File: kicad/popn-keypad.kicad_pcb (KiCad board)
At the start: 2 copper layers, 133.3 x 47.6 mm, 14 parts, among them U1 Arduino_Pro_Micro

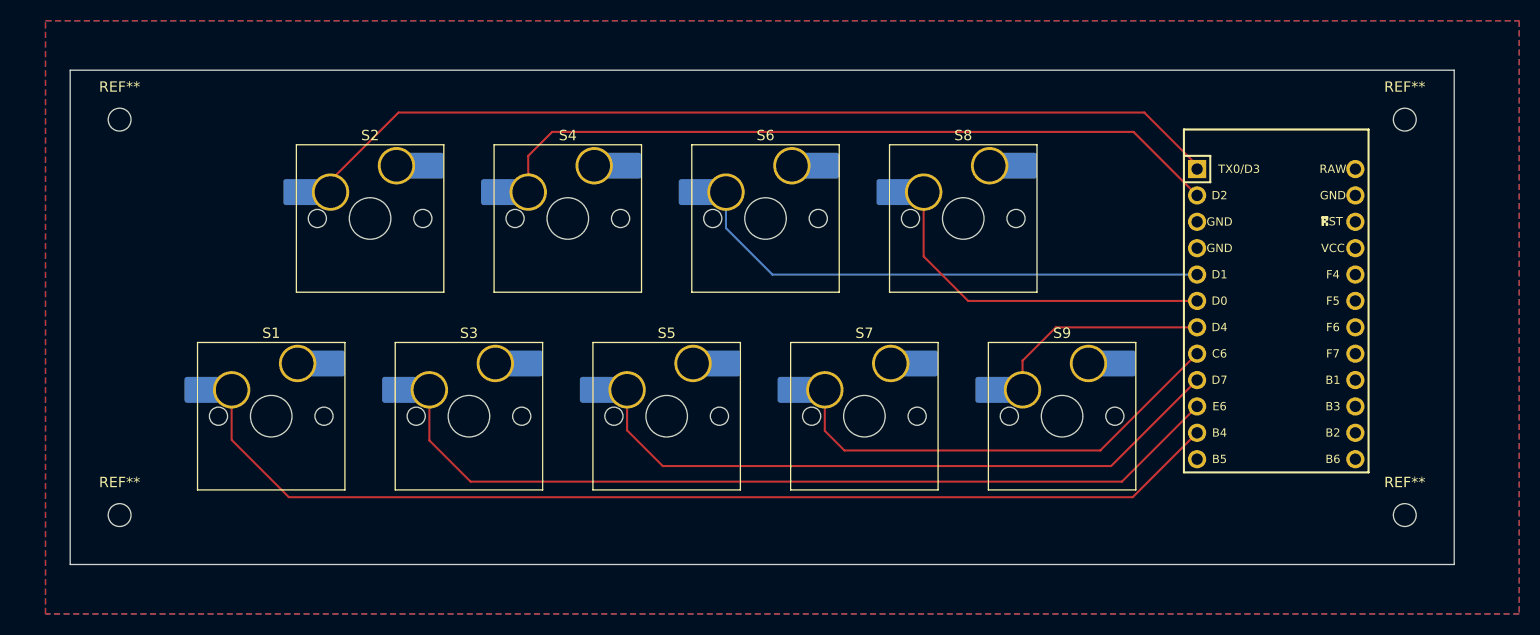
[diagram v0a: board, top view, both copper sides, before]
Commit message: Redesigned board
Moved the microcontroller farther away from the keys. Also re-routed my traces to be further from any holes on the board.
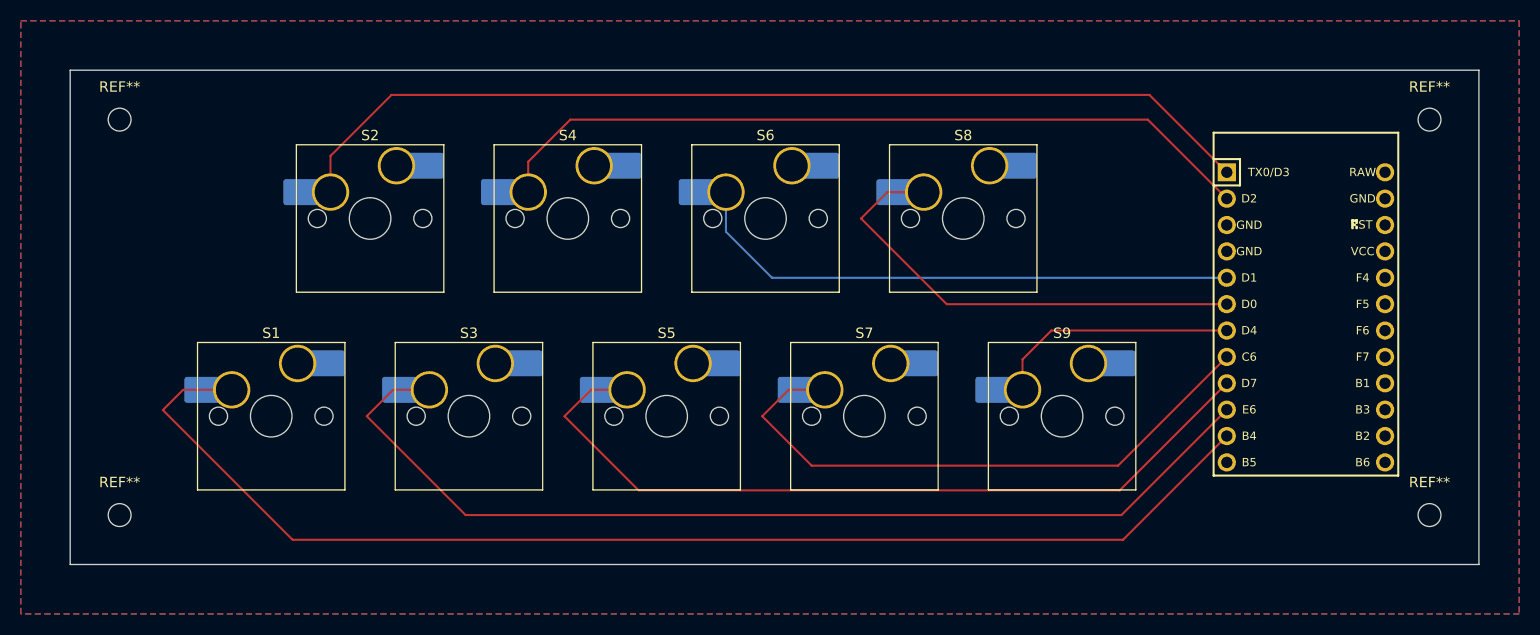
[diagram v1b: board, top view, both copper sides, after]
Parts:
- moved U1 2.88 mm to (209.4, 85.7)
- moved REF** 2.38 mm to (221.3, 66.6)
- moved REF** 2.38 mm to (221.3, 104.7)
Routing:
- net S9: track 102.7 -> 119.2 mm
- net S8: track 83.4 -> 98.0 mm
- net S7: track 63.7 -> 78.1 mm
- net S6: track 44.4 -> 58.1 mm
- net S4: track 34.3 -> 45.7 mm
- net S1: track 89.7 -> 96.4 mm
- net S2: track 71.4 -> 75.0 mm
- net S3: track 50.8 -> 53.9 mm
- net S5: track 20.9 -> 23.8 mm
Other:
- board size 133.3 x 47.6 mm -> 135.7 x 47.6 mm
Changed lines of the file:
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@@
 	(footprint "MountingHole:MountingHole_2.2mm_M2"
 		(layer "F.Cu")
-		(at 218.96 66.64)
+		(at 221.34 66.64)
 		(descr "Mounting Hole 2.2mm, M2, no annular, generated by kicad-footprint-generator mountinghole.py")
 		(tags "mountinghole M2")
@@
 	(footprint "ScottoKeebs_MCU:Arduino_Pro_Micro"
 		(layer "F.Cu")
-		(at 206.58 85.37)
+		(at 209.44 85.68)
 		(property "Reference" "U1"
 			(at 0 1.625 0)
@@
 	(footprint "MountingHole:MountingHole_2.2mm_M2"
 		(layer "F.Cu")
-		(at 218.96 104.72)
+		(at 221.34 104.72)
 		(descr "Mounting Hole 2.2mm, M2, no annular, generated by kicad-footprint-generator mountinghole.py")
 		(tags "mountinghole M2")
@@
 	(gr_rect
 		(start 90.44 61.88)
-		(end 223.72 109.48)
+		(end 226.1 109.48)
 		(stroke
 			(width 0.05)
@@
 	)
 	(segment
-		(start 115.51 72.51)
-		(end 122.062796 65.957204)
+		(start 115.51 73.62)
+		(end 115.51 70.13)
 		(width 0.2)
 		(layer "F.Cu")
@@
 	)
 	(segment
-		(start 193.876204 65.957204)
-		(end 198.96 71.041)
+		(start 121.38 64.26)
+		(end 194.37 64.26)
 		(width 0.2)
 		(layer "F.Cu")
@@
 	)
 	(segment
-		(start 122.062796 65.957204)
-		(end 193.876204 65.957204)
+		(start 115.51 70.13)
+		(end 121.38 64.26)
 		(width 0.2)
 		(layer "F.Cu")
@@
 	)
 	(segment
-		(start 198.96 71.041)
-		(end 198.96 71.4)
+		(start 194.37 64.26)
+		(end 201.82 71.71)
 		(width 0.2)
 		(layer "F.Cu")
@@
 	)
 	(segment
-		(start 153.59 73.62)
-		(end 153.59 77.09)
+		(start 158.03 81.87)
+		(end 201.82 81.87)
 		(width 0.2)
 		(layer "B.Cu")
@@
 	)
 	(segment
-		(start 153.59 77.09)
-		(end 158.06 81.56)
+		(start 153.59 73.62)
+		(end 153.59 77.43)
 		(width 0.2)
 		(layer "B.Cu")
@@
 	)
 	(segment
-		(start 158.06 81.56)
-		(end 198.96 81.56)
+		(start 153.59 77.43)
+		(end 158.03 81.87)
 		(width 0.2)
 		(layer "B.Cu")
@@
 	)
 	(segment
-		(start 182.15 89.85)
-		(end 185.36 86.64)
+		(start 182.15 89.725)
+		(end 184.925 86.95)
 		(width 0.2)
 		(layer "F.Cu")
@@
 	(segment
 		(start 182.15 92.66)
-		(end 182.15 89.85)
+		(end 182.15 89.725)
 		(width 0.2)
 		(layer "F.Cu")
@@
 	)
 	(segment
-		(start 185.36 86.64)
-		(end 198.96 86.64)
+		(start 184.925 86.95)
+		(end 201.82 86.95)
 		(width 0.2)
 		(layer "F.Cu")
@@
 	)
 	(segment
-		(start 147.5 100)
-		(end 144.07 96.57)
+		(start 138.04 95.2)
+		(end 140.58 92.66)
 		(width 0.2)
 		(layer "F.Cu")
@@
 	)
 	(segment
-		(start 198.96 91.72)
-		(end 190.68 100)
+		(start 201.82 92.03)
+		(end 191.51 102.34)
 		(width 0.2)
 		(layer "F.Cu")
@@
 	)
 	(segment
-		(start 190.68 100)
-		(end 147.5 100)
+		(start 140.58 92.66)
+		(end 144.07 92.66)
 		(width 0.2)
 		(layer "F.Cu")
@@
 	)
 	(segment
-		(start 144.07 96.57)
-		(end 144.07 92.66)
+		(start 145.18 102.34)
+		(end 138.04 95.2)
+		(width 0.2)
+		(layer "F.Cu")
+		(net 5)
+	)
+	(segment
+		(start 191.51 102.34)
+		(end 145.18 102.34)
 		(width 0.2)
 		(layer "F.Cu")
@@
 	)
 	(segment
-		(start 192.76 103)
-		(end 111.5 103)
+		(start 99.365 94.605)
+		(end 101.31 92.66)
 		(width 0.2)
 		(layer "F.Cu")
@@
 	)
 	(segment
-		(start 111.5 103)
-		(end 105.99 97.49)
+		(start 111.86 107.1)
+		(end 99.365 94.605)
 		(width 0.2)
 		(layer "F.Cu")
@@
 	)
 	(segment
-		(start 198.96 96.8)
-		(end 192.76 103)
+		(start 201.82 97.11)
+		(end 191.83 107.1)
 		(width 0.2)
 		(layer "F.Cu")
@@
 	)
 	(segment
-		(start 105.99 97.49)
+		(start 191.83 107.1)
+		(end 111.86 107.1)
+		(width 0.2)
+		(layer "F.Cu")
+		(net 6)
+	)
+	(segment
+		(start 101.31 92.66)
 		(end 105.99 92.66)
 		(width 0.2)
@@
 	)
 	(segment
-		(start 136.856956 67.823044)
-		(end 192.843044 67.823044)
+		(start 134.55 73.62)
+		(end 134.55 70.685)
 		(width 0.2)
 		(layer "F.Cu")
@@
 	)
 	(segment
-		(start 192.843044 67.823044)
-		(end 198.96 73.94)
+		(start 134.55 70.685)
+		(end 138.595 66.64)
 		(width 0.2)
 		(layer "F.Cu")
@@
 	)
 	(segment
-		(start 134.55 73.62)
-		(end 134.55 70.13)
+		(start 138.595 66.64)
+		(end 194.21 66.64)
 		(width 0.2)
 		(layer "F.Cu")
@@
 	)
 	(segment
-		(start 134.55 70.13)
-		(end 136.856956 67.823044)
+		(start 194.21 66.64)
+		(end 201.82 74.25)
 		(width 0.2)
 		(layer "F.Cu")
@@
 	)
 	(segment
-		(start 172.63 79.81)
-		(end 176.92 84.1)
+		(start 169.14 73.62)
+		(end 172.63 73.62)
 		(width 0.2)
 		(layer "F.Cu")
@@
 	)
 	(segment
-		(start 176.92 84.1)
-		(end 198.96 84.1)
+		(start 166.6 76.16)
+		(end 169.14 73.62)
 		(width 0.2)
 		(layer "F.Cu")
@@
 	)
 	(segment
-		(start 172.63 73.62)
-		(end 172.63 79.81)
+		(start 201.82 84.41)
+		(end 174.85 84.41)
 		(width 0.2)
 		(layer "F.Cu")
@@
 	)
 	(segment
-		(start 163.11 96.61)
-		(end 163.11 92.66)
+		(start 174.85 84.41)
+		(end 166.6 76.16)
+		(width 0.2)
+		(layer "F.Cu")
+		(net 8)
+	)
+	(segment
+		(start 201.82 89.49)
+		(end 191.35 99.96)
 		(width 0.2)
 		(layer "F.Cu")
@@
 	)
 	(segment
-		(start 189.64 98.5)
-		(end 165 98.5)
+		(start 157.08 95.2)
+		(end 159.62 92.66)
 		(width 0.2)
 		(layer "F.Cu")
@@
 	)
 	(segment
-		(start 198.96 89.18)
-		(end 189.64 98.5)
+		(start 161.84 99.96)
+		(end 157.08 95.2)
 		(width 0.2)
 		(layer "F.Cu")
@@
 	)
 	(segment
-		(start 165 98.5)
-		(end 163.11 96.61)
+		(start 159.62 92.66)
+		(end 163.11 92.66)
 		(width 0.2)
 		(layer "F.Cu")
@@
 	)
 	(segment
-		(start 191.72 101.5)
-		(end 129 101.5)
+		(start 191.35 99.96)
+		(end 161.84 99.96)
 		(width 0.2)
 		(layer "F.Cu")
-		(net 10)
+		(net 9)
 	)
 	(segment
-		(start 125.03 97.53)
+		(start 121.54 92.66)
 		(end 125.03 92.66)
 		(width 0.2)
@@
 	)
 	(segment
-		(start 198.96 94.26)
-		(end 191.72 101.5)
+		(start 191.67 104.72)
+		(end 128.52 104.72)
+		(width 0.2)
+		(layer "F.Cu")
+		(net 10)
+	)
+	(segment
+		(start 201.82 94.57)
+		(end 191.67 104.72)
+		(width 0.2)
+		(layer "F.Cu")
+		(net 10)
+	)
+	(segment
+		(start 128.52 104.72)
+		(end 119 95.2)
 		(width 0.2)
 		(layer "F.Cu")
@@
 	)
 	(segment
-		(start 129 101.5)
-		(end 125.03 97.53)
+		(start 119 95.2)
+		(end 121.54 92.66)
 		(width 0.2)
 		(layer "F.Cu")
@@
 		(polygon
 			(pts
-				(xy 88.06 57.12) (xy 229.98 57.12) (xy 229.98 114.24) (xy 88.06 114.24)
+				(xy 85.68 57.12) (xy 229.98 57.12) (xy 229.98 114.24) (xy 85.68 114.24)
 			)
 		)

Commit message: Changed shopping list, made tweaks to files
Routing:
- net S9: track 119.2 -> 118.5 mm
- net S8: track 98.0 -> 97.5 mm
- net S6: track 58.1 -> 57.6 mm
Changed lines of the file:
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@@
 	)
 	(segment
-		(start 138.04 95.2)
-		(end 140.58 92.66)
+		(start 140.54 92.66)
+		(end 144.07 92.66)
 		(width 0.2)
 		(layer "F.Cu")
@@
 	)
 	(segment
-		(start 140.58 92.66)
-		(end 144.07 92.66)
-		(width 0.2)
-		(layer "F.Cu")
-		(net 5)
-	)
-	(segment
-		(start 145.18 102.34)
-		(end 138.04 95.2)
+		(start 144.24 102.34)
+		(end 138.3 96.4)
+		(width 0.2)
+		(layer "F.Cu")
+		(net 5)
+	)
+	(segment
+		(start 138.3 94.9)
+		(end 140.54 92.66)
+		(width 0.2)
+		(layer "F.Cu")
+		(net 5)
+	)
+	(segment
+		(start 138.3 96.4)
+		(end 138.3 94.9)
 		(width 0.2)
 		(layer "F.Cu")
@@
 	(segment
 		(start 191.51 102.34)
-		(end 145.18 102.34)
-		(width 0.2)
-		(layer "F.Cu")
-		(net 5)
-	)
-	(segment
-		(start 99.365 94.605)
-		(end 101.31 92.66)
+		(end 144.24 102.34)
+		(width 0.2)
+		(layer "F.Cu")
+		(net 5)
+	)
+	(segment
+		(start 191.83 107.1)
+		(end 111.86 107.1)
 		(width 0.2)
 		(layer "F.Cu")
@@
 	(segment
 		(start 111.86 107.1)
-		(end 99.365 94.605)
+		(end 100.2 95.44)
 		(width 0.2)
 		(layer "F.Cu")
@@
 	)
 	(segment
-		(start 191.83 107.1)
-		(end 111.86 107.1)
-		(width 0.2)
-		(layer "F.Cu")
-		(net 6)
-	)
-	(segment
 		(start 101.31 92.66)
 		(end 105.99 92.66)
@@
 	)
 	(segment
+		(start 100.2 93.77)
+		(end 101.31 92.66)
+		(width 0.2)
+		(layer "F.Cu")
+		(net 6)
+	)
+	(segment
+		(start 100.2 95.44)
+		(end 100.2 93.77)
+		(width 0.2)
+		(layer "F.Cu")
+		(net 6)
+	)
+	(segment
 		(start 134.55 73.62)
 		(end 134.55 70.685)
@@
 	)
 	(segment
-		(start 169.14 73.62)
+		(start 174.85 84.41)
+		(end 167.3 76.86)
+		(width 0.2)
+		(layer "F.Cu")
+		(net 8)
+	)
+	(segment
+		(start 168.98 73.62)
 		(end 172.63 73.62)
 		(width 0.2)
@@
 	)
 	(segment
-		(start 166.6 76.16)
-		(end 169.14 73.62)
+		(start 167.3 76.86)
+		(end 167.3 75.3)
 		(width 0.2)
 		(layer "F.Cu")
@@
 	)
 	(segment
-		(start 174.85 84.41)
-		(end 166.6 76.16)
-		(width 0.2)
-		(layer "F.Cu")
-		(net 8)
+		(start 167.3 75.3)
+		(end 168.98 73.62)
+		(width 0.2)
+		(layer "F.Cu")
+		(net 8)
+	)
+	(segment
+		(start 161.84 99.96)
+		(end 157.7 95.82)
+		(width 0.2)
+		(layer "F.Cu")
+		(net 9)
 	)
 	(segment
@@
 	)
 	(segment
-		(start 157.08 95.2)
-		(end 159.62 92.66)
-		(width 0.2)
-		(layer "F.Cu")
-		(net 9)
-	)
-	(segment
-		(start 161.84 99.96)
-		(end 157.08 95.2)
-		(width 0.2)
-		(layer "F.Cu")
-		(net 9)
-	)
-	(segment
 		(start 159.62 92.66)
 		(end 163.11 92.66)
@@
 	)
 	(segment
+		(start 157.7 95.82)
+		(end 157.7 94.58)
+		(width 0.2)
+		(layer "F.Cu")
+		(net 9)
+	)
+	(segment
 		(start 191.35 99.96)
 		(end 161.84 99.96)
@@
 	)
 	(segment
+		(start 157.7 94.58)
+		(end 159.62 92.66)
+		(width 0.2)
+		(layer "F.Cu")
+		(net 9)
+	)
+	(segment
+		(start 201.82 94.57)
+		(end 191.67 104.72)
+		(width 0.2)
+		(layer "F.Cu")
+		(net 10)
+	)
+	(segment
+		(start 191.67 104.72)
+		(end 128.52 104.72)
+		(width 0.2)
+		(layer "F.Cu")
+		(net 10)
+	)
+	(segment
+		(start 119.7 94.5)
+		(end 121.54 92.66)
+		(width 0.2)
+		(layer "F.Cu")
+		(net 10)
+	)
+	(segment
+		(start 119.7 95.9)
+		(end 119.7 94.5)
+		(width 0.2)
+		(layer "F.Cu")
+		(net 10)
+	)
+	(segment
+		(start 128.52 104.72)
+		(end 119.7 95.9)
+		(width 0.2)
+		(layer "F.Cu")
+		(net 10)
+	)
+	(segment
 		(start 121.54 92.66)
 		(end 125.03 92.66)
 		(width 0.2)
 		(layer "F.Cu")
-		(net 10)
-	)
-	(segment
-		(start 191.67 104.72)
-		(end 128.52 104.72)
-		(width 0.2)
-		(layer "F.Cu")
-		(net 10)
-	)
-	(segment
-		(start 201.82 94.57)
-		(end 191.67 104.72)
-		(width 0.2)
-		(layer "F.Cu")
-		(net 10)
-	)
-	(segment
-		(start 128.52 104.72)
-		(end 119 95.2)
-		(width 0.2)
-		(layer "F.Cu")
-		(net 10)
-	)
-	(segment
-		(start 119 95.2)
-		(end 121.54 92.66)
-		(width 0.2)
-		(layer "F.Cu")

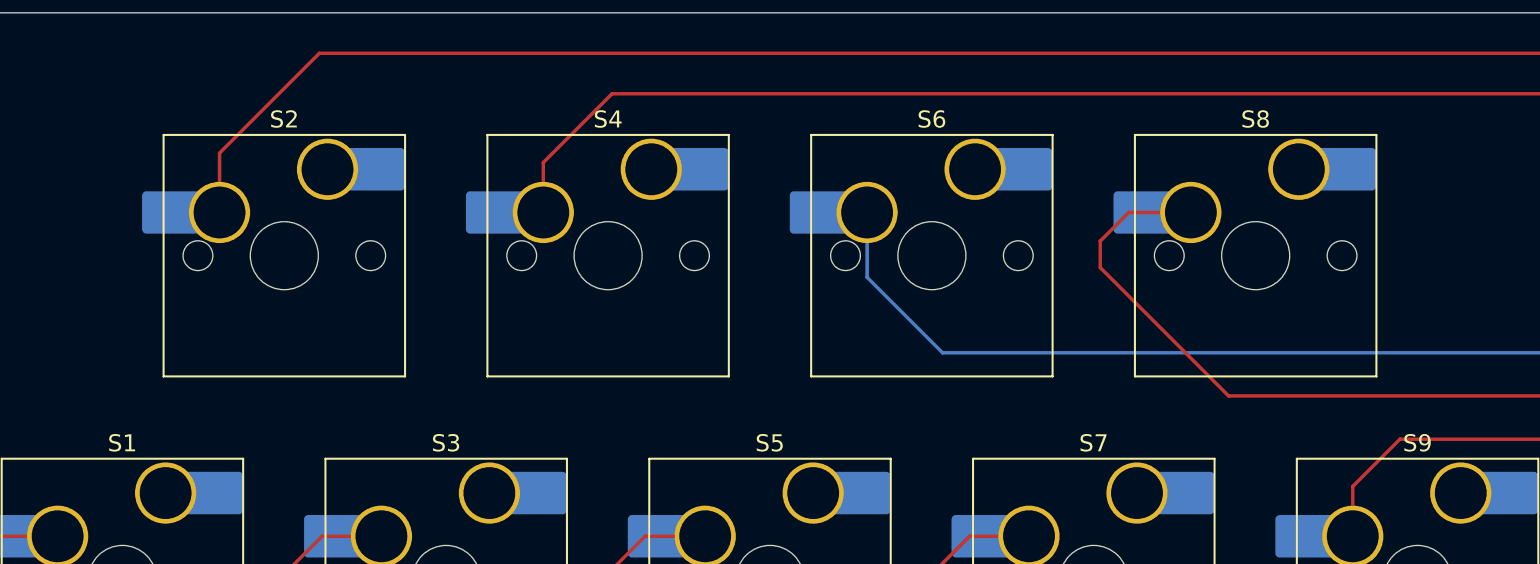
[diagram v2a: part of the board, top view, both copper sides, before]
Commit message: Updated to Kicad 10, renamed some parts for organization
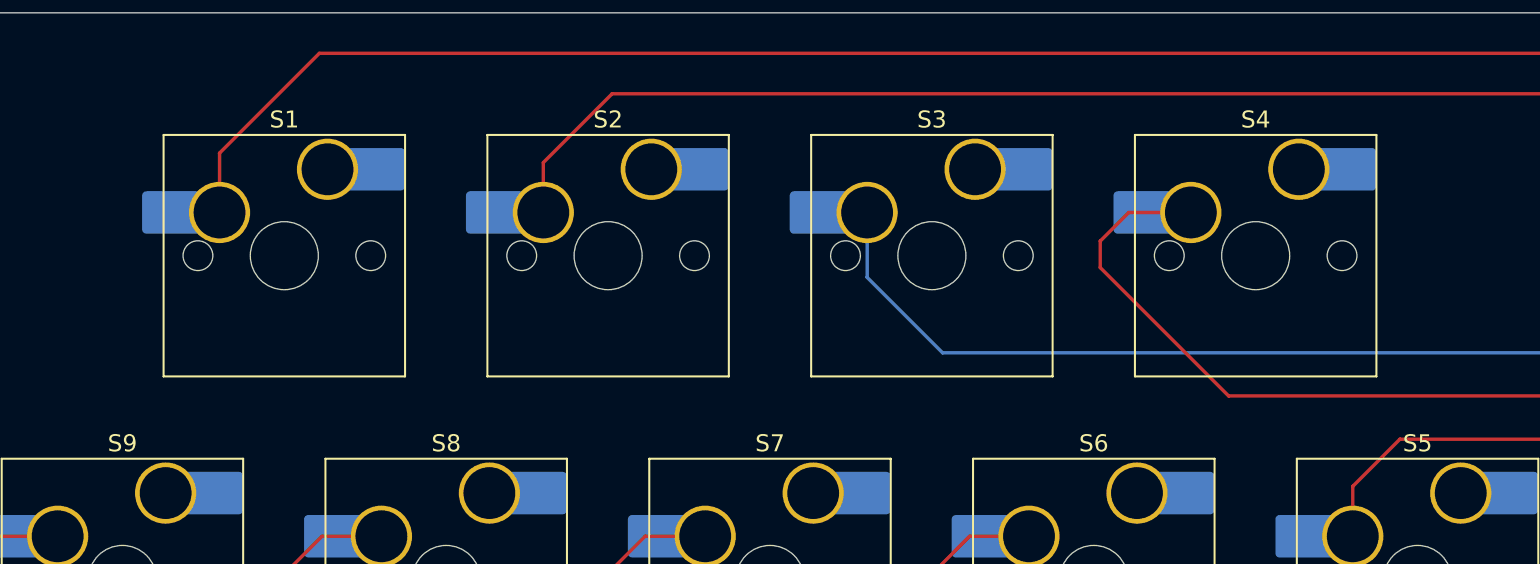
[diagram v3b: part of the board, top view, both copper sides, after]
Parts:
- renumbered S2 to S1, S4 to S2, S6 to S3, S8 to S4, S9 to S5, S7 to S6, S5 to S7, S3 to S8, S1 to S9
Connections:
- U1 pad 23: unconnected-(U1-GND-Pad23) -> GND
